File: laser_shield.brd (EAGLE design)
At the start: 100 x 81.3 mm, 36 parts, among them Q1 IRF3704S, Q2 IRF3704S, U1 ARDUINO_SHIELDLONGPADS

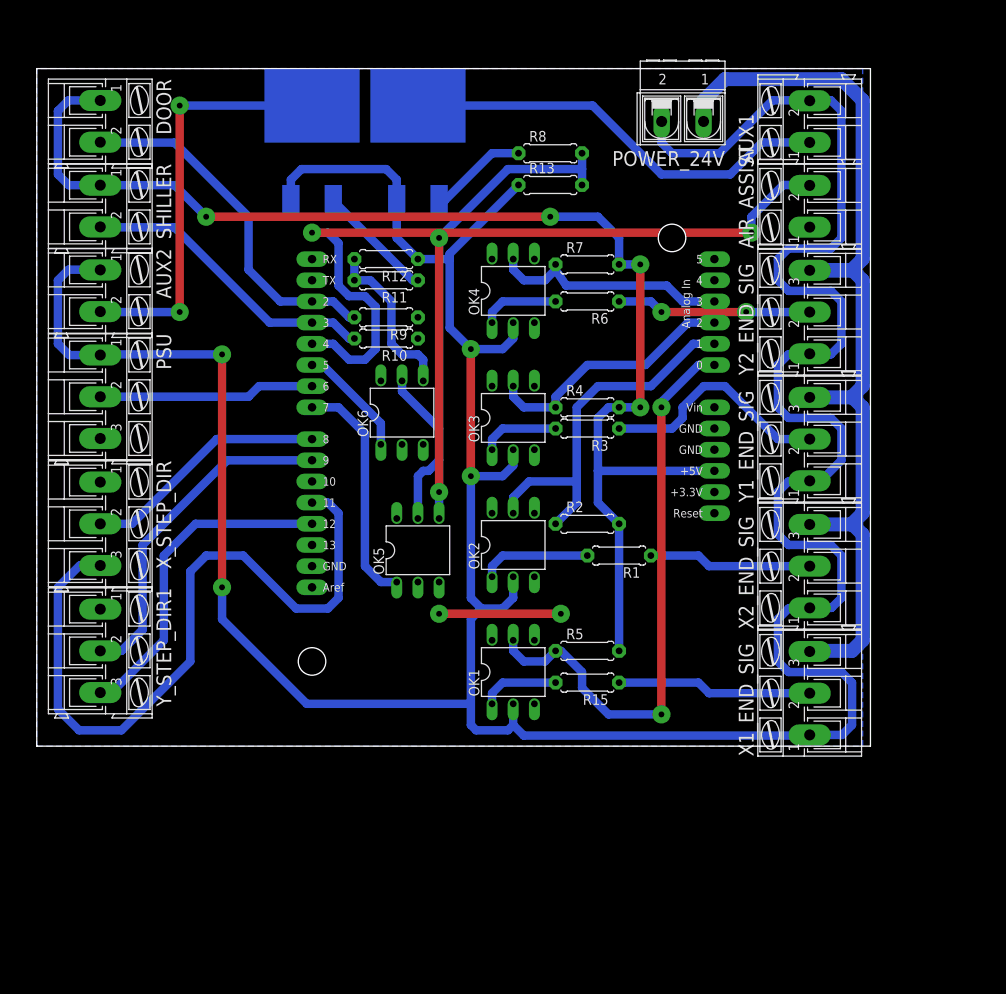
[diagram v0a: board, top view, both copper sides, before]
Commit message: Modified for regular GRBL
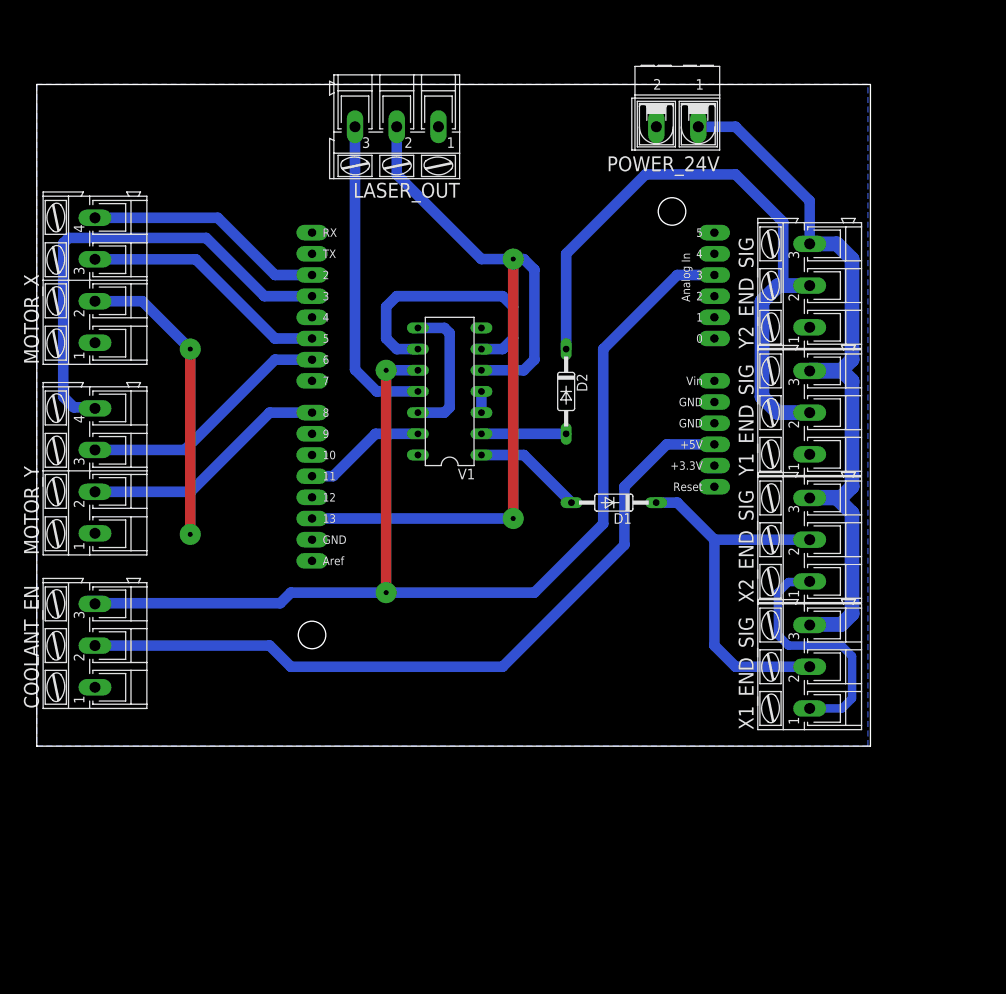
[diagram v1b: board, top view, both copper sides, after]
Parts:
- removed AIR_ASSIST, AUX1, AUX2, DOOR, SHILLER: (no value), con-ptr500:AK300/2
- removed OK1, OK2, OK3, OK4, OK5, OK6: 4N35, optocoupler:DIL06
- removed PSU, X_STEP_DIR, Y_STEP_DIR1: (no value), con-ptr500:AK300/3
- removed Q1, Q2: IRF3704S, transistor-power:D2PACK
- removed R1, R15, R3, R6: 330 Ohm, rcl:0207/7
- removed R10, R2, R4, R9: 10K, rcl:0207/7
- removed R11, R8: 1K, rcl:0207/7
- removed R12, R13: 220K, rcl:0207/7
- removed R5, R7: 10k, rcl:0207/7
- added COOLANT_EN, LASER_OUT: (no value), con-ptr500:AK300/3
- added D1, D2: 1N4148DO35-10, diode:DO35-10
- added MOTOR_X, MOTOR_Y: (no value), con-ptr500:AK300/4
- added V1: 7408N, 74ttl-din:DIL14
- moved Y1_END_SIG 3.18 mm to (92.7, 40.0)
- moved X1_END_SIG 3.18 mm to (92.7, 9.53)
- moved X2_END_SIG 3.18 mm to (92.7, 24.8)
- moved U1 3.18 mm to (30.5, 6.99)
- moved Y2_END_SIG 3.17 mm to (92.7, 55.2)
- moved POWER_24V 0.90 mm to (76.8, 74.3)
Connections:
- net Z1_END_STOP renamed NC
- net Z2_END_STOP renamed PROBE*
- removed net AIR_ASSIST: AIR_ASSIST.2, U1.D4
- removed net ARDUINO_5V: DOOR.1, R2.2, R4.2, R5.2, R7.2, SHILLER.1, U1.5V
- removed net AUX1_ASSIST: OK5.1, U1.D7
- removed net AUX2_ASSIST: OK6.1, U1.D5
- removed net AUX_1: AUX1.1, Q2.2
- removed net AUX_2: AUX2.2, Q1.2
- removed net DOOR_STATE: DOOR.2, R9.2, U1.D2
- removed net GND_24: AUX1.2, AUX2.1, OK1.2, OK2.2, OK3.2, OK4.2, POWER_24V.2, PSU.1, Q1.3, Q2.3, R12.1, R13.1, X1_END_SIG.1, X2_END_SIG.1, Y1_END_SIG.1, Y2_END_SIG.1
- removed net N$6: OK5.4, R13.2, R8.2
- removed net N$8: Q1.1, R11.1
- removed net N$9: OK6.4, R11.2, R12.2
- removed net PSU_PWM: PSU.2, U1.D6
- removed net PSU_STATE: PSU.3
- removed net SHILLER_STATE: R10.2, SHILLER.2, U1.D3
- removed net VCC_24V: OK5.5, OK6.5
- removed net X1_END_SIG: R15.1, X1_END_SIG.2
- removed net X1_END_STOP: OK1.5, R5.1, U1.A0
- removed net X2_END_SIG: R1.1, X2_END_SIG.2
- removed net X2_END_STOP: OK2.5, R2.1, U1.A1
- removed net Y1_END_SIG: R3.1, Y1_END_SIG.2
- removed net Y1_END_STOP: OK3.5, R4.1, U1.A2
- removed net Y2_END_SIG: R6.1, Y2_END_SIG.2
- removed net Y2_END_STOP: OK4.5, R7.1, U1.A3
- new net +UB: V1.14
- new net -UB: V1.7
- new net COOLANT_EN: COOLANT_EN.3, U1.A3, V1.10
- new net CYCLE-START*: U1.A2
- new net FEED_HOLD*: U1.A1
- new net LASER_PWM_OUT: LASER_OUT.3, V1.11
- new net LIMIT_X: U1.D9
- new net LIMIT_Y: U1.D10
- new net LIMIT_Z: U1.D12
- new net RESET*: U1.A0
- new net SPINDLE_DIR: LASER_OUT.2, U1.D13, V1.5
- new net SPINDLE_PWM: U1.D11, V1.13
- new net STEP_EN: MOTOR_X.2, MOTOR_Y.2, U1.D8
- new net VCC: COOLANT_EN.2, U1.5V
- new net X_END_STOP: D1.C, X1_END_SIG.2, X2_END_SIG.2
- new net Y_END_STOP: D2.C, Y1_END_SIG.2, Y2_END_SIG.2
- net GND: now also COOLANT_EN.1, LASER_OUT.1, MOTOR_X.1, MOTOR_Y.1, POWER_24V.2, X1_END_SIG.1, X2_END_SIG.1, Y1_END_SIG.1, Y2_END_SIG.1; no longer AIR_ASSIST.1, OK1.4, OK2.4, OK3.4, OK4.4, OK5.2, OK6.2, R10.1, R9.1, X_STEP_DIR.1, Y_STEP_DIR1.1
- net N$1: now also D1.A, V1.1; no longer OK2.1, R1.2
- net N$2: now also D2.A, V1.2; no longer OK3.1, R3.2
- net N$3: now also V1.3, V1.4; no longer OK4.1, R6.2
- net N$4: now also V1.6, V1.9; no longer Q2.1, R8.1
- net N$5: now also V1.12, V1.8; no longer OK1.1, R15.2
- net X_DIR: now also MOTOR_X.3, U1.D5; no longer U1.D11, X_STEP_DIR.3
- net X_STEP: now also MOTOR_X.4, U1.D2; no longer U1.D8, X_STEP_DIR.2
- net Y_DIR: now also MOTOR_Y.3, U1.D6; no longer U1.D12, Y_STEP_DIR1.3
- net Y_STEP: now also MOTOR_Y.4, U1.D3; no longer U1.D9, Y_STEP_DIR1.2
- net Z_DIR: now also U1.D7; no longer U1.D13
- net Z_STEP: now also U1.D4; no longer U1.D10
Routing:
- net GND_24: track 423.2 -> 0.00 mm, vias 4 -> 0
- net ARDUINO_5V: track 155.1 -> 0.00 mm, vias 4 -> 0
- net COOLANT_EN: track 0.00 -> 133.4 mm, vias 0 -> 2
- net SPINDLE_DIR: track 0.00 -> 99.9 mm, vias 0 -> 2
- net AIR_ASSIST: track 91.5 -> 0.00 mm, vias 2 -> 0
- net VCC: track 0.00 -> 90.5 mm
- net Y_END_STOP: track 0.00 -> 76.1 mm
- net STEP_EN: track 0.00 -> 71.1 mm, vias 0 -> 2
- net X1_END_STOP: track 70.0 -> 0.00 mm, vias 2 -> 0
- net N$6: track 58.0 -> 0.00 mm, vias 2 -> 0
- net X_DIR: track 87.5 -> 30.0 mm
- net AUX_1: track 52.0 -> 0.00 mm
- net AUX_2: track 50.2 -> 0.00 mm, vias 2 -> 0
- net X_END_STOP: track 0.00 -> 45.4 mm
- net X2_END_STOP: track 45.0 -> 0.00 mm
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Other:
- board size 100 x 81.3 mm -> 100 x 79.4 mm

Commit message: Added new connectors
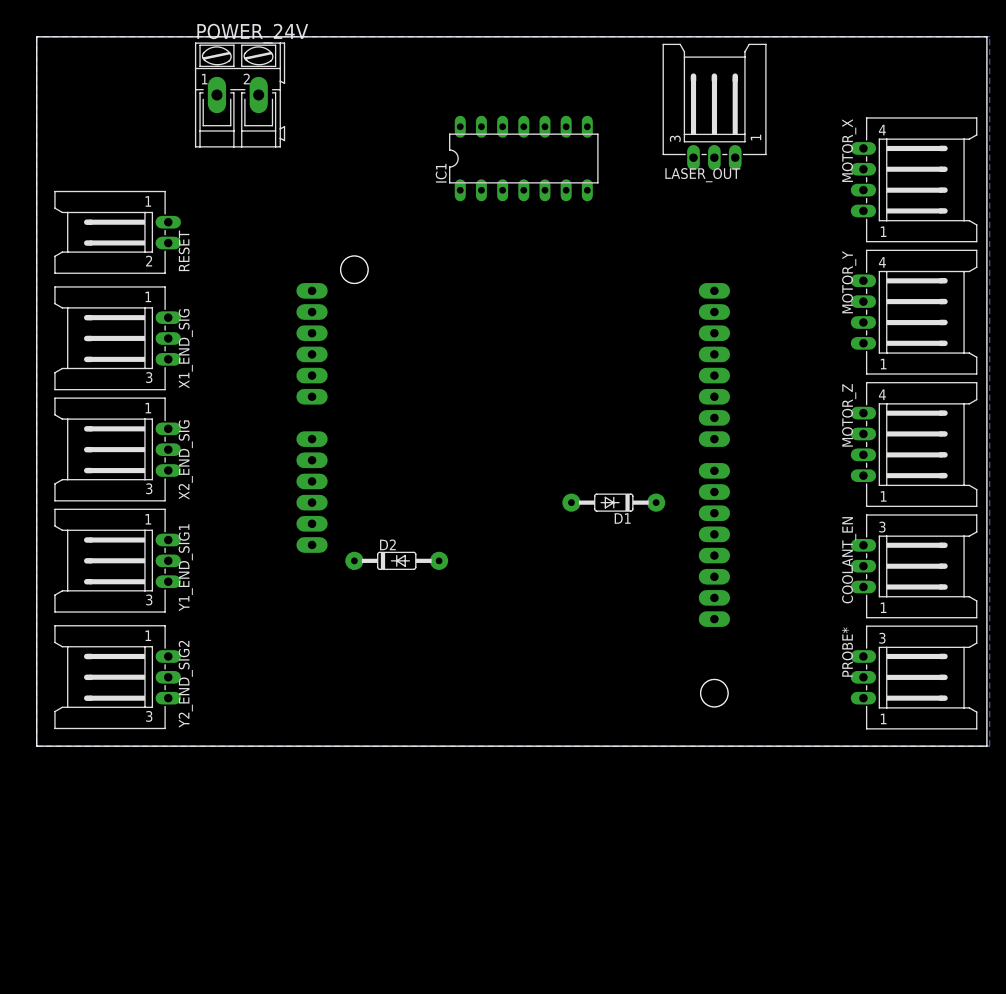
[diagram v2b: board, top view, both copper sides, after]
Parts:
- removed V1: 7408N, 74ttl-din:DIL14
- removed Y1_END_SIG, Y2_END_SIG: (no value), con-ptr500:AK300/3
- added IC1: 74AC08N, 74xx-eu:DIL14
- added MOTOR_Z: (no value), con-amp-mt:L04P
- added PROBE*, Y1_END_SIG1, Y2_END_SIG2: (no value), con-amp-mt:L03P
- added RESET: (no value), con-amp-mt:L02P
- COOLANT_EN, LASER_OUT, X1_END_SIG, X2_END_SIG: device con-ptr500:AK300/3 -> con-amp-mt:L03P
- MOTOR_X, MOTOR_Y: device con-ptr500:AK300/4 -> con-amp-mt:L04P
- POWER_24V: device con-ptr500:AK500/2-H -> con-ptr500:AK300/2
- moved MOTOR_Y 100.3 mm to (105.4, 52.1), turned to 270 degrees
- moved MOTOR_X 99.2 mm to (105.4, 67.9), turned to 270 degrees
- moved COOLANT_EN 98.9 mm to (105.4, 21.6), turned to 270 degrees
- moved X1_END_SIG 92.0 mm to (9.53, 48.9)
- moved X2_END_SIG 83.9 mm to (9.53, 35.6)
- moved U1 53.8 mm to (83.8, 0.00), flipped to the bottom
- moved POWER_24V 52.8 mm to (24.1, 78.1), turned to 0 degrees
- moved LASER_OUT 38.2 mm to (81.3, 76.8), turned to 0 degrees
- moved D2 28.7 mm to (43.2, 22.2), turned to 0 degrees
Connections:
- removed net +UB: V1.14
- removed net -UB: V1.7
- removed net N$1: D1.A, V1.1
- removed net N$2: D2.A, V1.2
- new net PROB*: PROBE*.2
- net COOLANT_EN: now also IC1.10; no longer V1.10
- net GND: now also IC1.7, MOTOR_Z.1, PROBE*.1, RESET.1, X1_END_SIG.3, X2_END_SIG.3, Y1_END_SIG1.3, Y2_END_SIG2.3; no longer X1_END_SIG.1, X2_END_SIG.1, Y1_END_SIG.1, Y2_END_SIG.1
- net LASER_PWM_OUT: now also IC1.11; no longer V1.11
- net LIMIT_X: now also D1.A, IC1.1
- net LIMIT_Y: now also D2.A, IC1.2
- net N$3: now also IC1.3, IC1.4; no longer V1.3, V1.4
- net N$4: now also IC1.6, IC1.9; no longer V1.6, V1.9
- net N$5: now also IC1.12, IC1.8; no longer V1.12, V1.8
- net RESET*: now also RESET.2
- net SPINDLE_DIR: now also IC1.5; no longer V1.5
- net SPINDLE_PWM: now also IC1.13; no longer V1.13
- net STEP_EN: now also MOTOR_Z.2
- net VCC: now also IC1.14, PROBE*.3
- net VCC_24: now also X1_END_SIG.1, X2_END_SIG.1, Y1_END_SIG1.1, Y2_END_SIG2.1; no longer X1_END_SIG.3, X2_END_SIG.3, Y1_END_SIG.3, Y2_END_SIG.3
- net Y_END_STOP: now also Y1_END_SIG1.2, Y2_END_SIG2.2; no longer Y1_END_SIG.2, Y2_END_SIG.2
- net Z_DIR: now also MOTOR_Z.3
- net Z_STEP: now also MOTOR_Z.4
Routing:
- net COOLANT_EN: track 133.4 -> 0.00 mm, vias 2 -> 0
- net SPINDLE_DIR: track 99.9 -> 0.00 mm, vias 2 -> 0
- net VCC_24: track 97.2 -> 0.00 mm
- net VCC: track 90.5 -> 0.00 mm
- net Y_END_STOP: track 76.1 -> 0.00 mm
- net STEP_EN: track 71.1 -> 0.00 mm, vias 2 -> 0
- net Y_STEP: track 55.8 -> 0.00 mm
- net X_END_STOP: track 45.4 -> 0.00 mm
- net LASER_PWM_OUT: track 37.8 -> 0.00 mm
- net N$4: track 32.6 -> 0.00 mm
- net Y_DIR: track 30.5 -> 0.00 mm
- net X_DIR: track 30.0 -> 0.00 mm
- net GND: track 29.9 -> 0.00 mm
- net X_STEP: track 28.9 -> 0.00 mm
- net N$5: track 17.0 -> 0.00 mm
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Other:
- board size 100 x 79.4 mm -> 114 x 85.1 mm

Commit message: New rooting
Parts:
- added CYCLE_S, FEED_H: (no value), con-amp-mt:L02P
- moved D1 47.1 mm to (23.5, 40.6), turned to 90 degrees
- moved D2 20.3 mm to (23.5, 17.1), turned to 270 degrees
- moved POWER_24V 13.7 mm to (10.8, 74.9), turned to 90 degrees
- moved LASER_OUT 2.01 mm to (83.2, 76.2)
- moved IC1 1.80 mm to (59.7, 69.2)
- moved Y2_END_SIG2 0.63 mm to (9.53, 8.89)
- moved RESET 0.63 mm to (9.53, 61.0)
- renumbered PROBE* to PROBE
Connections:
- removed net CYCLE-START*: U1.A2
- removed net PROB*: PROBE.2
- new net CYCLE_START*: CYCLE_S.2, U1.A2
- net FEED_HOLD*: now also FEED_H.2
- net GND: now also CYCLE_S.1, FEED_H.1
- net PROBE*: now also PROBE.2
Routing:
- net VCC: track 0.00 -> 145.7 mm
- net COOLANT_EN: track 0.00 -> 140.2 mm, vias 0 -> 1
- net SPINDLE_PWM: track 0.00 -> 124.3 mm
- net PROBE*: track 0.00 -> 108.8 mm
- net LIMIT_Y: track 0.00 -> 106.8 mm, vias 0 -> 2
- net LIMIT_X: track 0.00 -> 93.6 mm
- net SPINDLE_DIR: track 0.00 -> 76.0 mm
- net VCC_24: track 0.00 -> 74.6 mm
- net STEP_EN: track 0.00 -> 58.6 mm
- net X_DIR: track 0.00 -> 45.0 mm
- net FEED_HOLD*: track 0.00 -> 40.1 mm
- net X_STEP: track 0.00 -> 37.1 mm
- net CYCLE_START*: track 0.00 -> 27.9 mm
- net Y_END_STOP: track 0.00 -> 27.3 mm
- net Y_DIR: track 0.00 -> 26.6 mm
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- added copper zone on layer 1, net GND
